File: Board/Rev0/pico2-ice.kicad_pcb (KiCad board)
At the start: 4 copper layers, 27.9 x 63.5 mm, 119 parts, among them J1 USB_C_Receptacle_USB2.0, J2 Conn_02x20_Odd_Even, J3 Conn_02x20_Odd_Even, J4 PB_SEL, J5 SM03B-SRSS-TB, J6 Conn_01x22_MountingPin, SW1 PTS820 J25K SMTR LFS, SW2 PTS820 J25K SMTR LFS, U1 NCP115AMX120TCG, U2 W25Q32JVSSIQ, U3 RP2350_80QFN, U4 TL431DBZ, U5 APS6404L-3SQN-SN, U6 ICE40UP5K-SG48ITR, U8 W25Q32JVSSIQ, U9 NCP115AMX330TCG, Y1 ABM8-272-T3

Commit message: Update the design with feedbacks.
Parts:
- SW1, SW2: value PTS820 J25K SMTR LFS -> CS1213AGF260
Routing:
- net GND: track 76.8 -> 78.0 mm, vias 73 -> 71

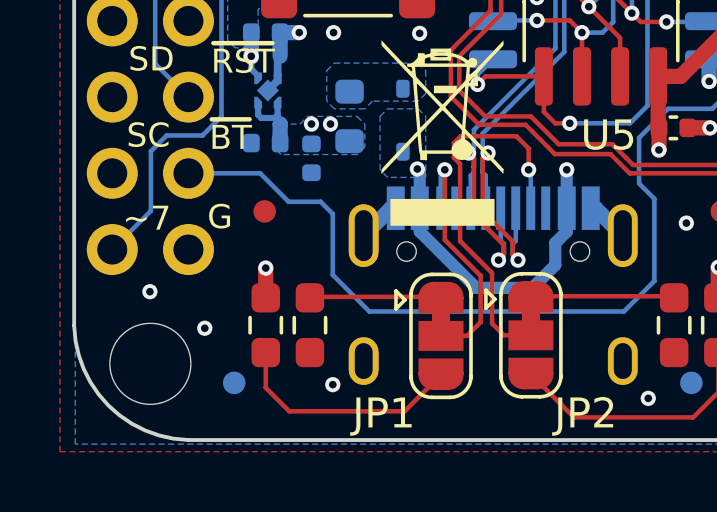
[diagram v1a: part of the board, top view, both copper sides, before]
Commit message: Minor silkscreen edits
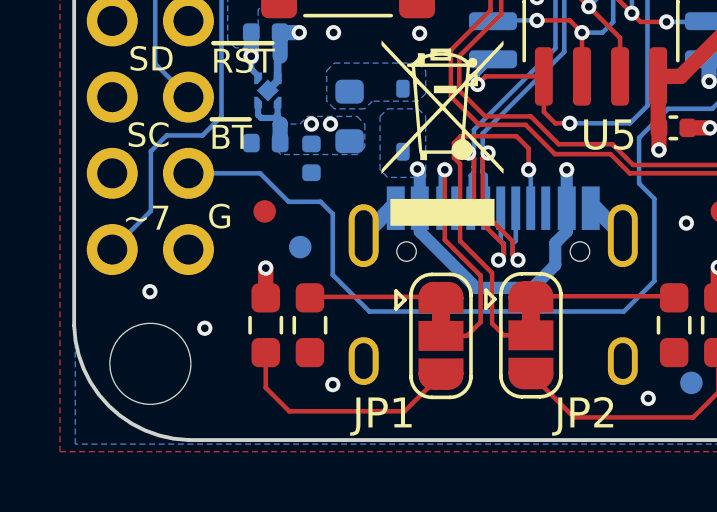
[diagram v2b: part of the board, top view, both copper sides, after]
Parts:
- moved FID6 5.03 mm to (66.0, 128.2)
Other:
- board text added: "pico2-ice"
- board text added: "rev1"
- board text removed: "pico-ice"
- board text removed: "pico-ice v1"
- board text removed: "rev3"
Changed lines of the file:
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@@
 	(footprint "Fiducial:Fiducial_0.75mm_Mask1.5mm"
 		(layer "B.Cu")
-		(at 63.754 132.715 180)
+		(at 65.955718 128.189071 180)
 		(descr "Circular Fiducial, 0.75mm bare copper, 1.5mm soldermask opening (Level B)")
 		(tags "fiducial")
@@
 		)
 	)
-	(gr_text "pico-ice"
-		(at 66.024918 130.386271 270)
+	(gr_text "pico2-ice"
+		(at 63.955718 130.689071 90)
 		(layer "B.Mask")
 		(effects
 			(font
-				(size 1.016 1.016)
-				(thickness 0.254)
-				(bold yes)
+				(size 0.9 0.9)
+				(thickness 0.127)
 			)
 			(justify mirror)
 		)
 	)
-	(gr_text "rev3"
-		(at 64.450118 129.167071 270)
+	(gr_text "rev1"
+		(at 65.955718 131.189071 90)
 		(layer "B.Mask")
 		(effects
 			(font
-				(size 1.016 1.016)
-				(thickness 0.254)
-				(bold yes)
+				(size 0.9 0.9)
+				(thickness 0.127)
 			)
 			(justify mirror)
 		)
 	)
-	(gr_text "pico-ice v1"
+	(gr_text "pico2-ice"
 		(at 78.470918 76.385871 0)
 		(layer "F.Mask")
@@
 			(font
 				(size 0.9 0.9)
-				(thickness 0.225)
-				(bold yes)
+				(thickness 0.1125)
 			)
 		)

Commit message: Sync the latest files.
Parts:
- removed J4: PB_SEL, Jumper:SolderJumper-3_P1.3mm_Bridged12_RoundedPad1.0x1.5mm_NumberLabels
- removed R14: 2.2K, Resistor_SMD:R_0402_1005Metric
- added D6: 1N5819WS, Diode_SMD:D_SOD-323, F.Cu at (96.1, 109.9)
- added R32: 10K, Resistor_SMD:R_0402_1005Metric, F.Cu at (92.4, 109.4)
- added R33: 5.1K, Resistor_SMD:R_0603_1608Metric_Pad0.98x0.95mm_HandSolder, F.Cu at (96.1, 112.6)
- added R34: 27, Resistor_SMD:R_0402_1005Metric, F.Cu at (92.4, 111.4)
- C13, C32, D2, D3, D4, J1, RN1, SW1, SW2: moved to F.Cu
- JP1, JP2, U8: moved to B.Cu
- R30, R31: footprint Resistor_SMD:R_0402_1005Metric -> Jumper:SolderJumper-2_P1.3mm_Bridged_RoundedPad1.0x1.5mm
- moved SW1 25.4 mm to (67.7, 122.8)
- moved LOGO3 24.0 mm to (97.1, 82.9)
- moved R30 23.0 mm to (95.2, 120.2)
- moved R31 22.6 mm to (95.3, 117.3)
- moved LOGO2 21.3 mm to (91.4, 129.2)
- moved LOGO4 15.9 mm to (92.6, 137.3)
- moved LOGO1 14.9 mm to (92.6, 72.4)
- moved FID3 14.3 mm to (57.4, 139.2)
- moved FID1 13.1 mm to (84.9, 139.1)
- moved FID6 12.3 mm to (60.4, 139.1)
- moved FID5 8.94 mm to (54.8, 74.3)
- moved JP2 8.86 mm to (73.4, 140.0)
- moved C26 8.84 mm to (73.9, 76.4), turned to 0 degrees
- moved JP1 8.27 mm to (67.5, 138.8)
- moved FID4 7.27 mm to (82.6, 139.0)
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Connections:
- J6 pad 11: /Lane2_N -> /Lane2_P
- J6 pad 12: /Lane2_P -> /Lane2_N
- R2 pad 2: /~{USB_BOOT} -> Net-(D6-A)
- R27 pad 2: /~{RP_SRAM_SS} -> /~{SRAM_SS}
- SW1 pad 2: Net-(J4-Pin_2) -> /~{USB_BOOT}
- U3 pad 11: /Lane2_N -> /Lane2_P
- U3 pad 12: /Lane2_P -> /Lane2_N
- U3 pad 22: /ICE_21 -> Net-(U3-GPIO22)
- U3 pad 27: /ICE_20_G3 -> /ICE_21
- U3 pad 36: /PICO_PMOD_A3 -> /ICE_9
- U3 pad 37: /PICO_PMOD_A1 -> /ICE_11
- U3 pad 38: /PICO_PMOD_A4 -> /ICE_25
- U3 pad 39: /PICO_PMOD_A2 -> /~{ICE_RST}
- U3 pad 40: /PICO_PMOD_B3 -> /PICO_PMOD_A3
- U3 pad 42: /PICO_PMOD_B1 -> /PICO_PMOD_A1
- U3 pad 43: /PICO_PMOD_B4 -> /PICO_PMOD_A4
- U3 pad 44: /PICO_PMOD_B2 -> /PICO_PMOD_A2
- U3 pad 45: /ICE_9 -> /PICO_PMOD_B3
- U3 pad 46: /ICE_11 -> /PICO_PMOD_B1
- U3 pad 47: /ICE_25 -> /PICO_PMOD_B4
- U3 pad 48: /~{ICE_RST} -> /PICO_PMOD_B2
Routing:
- net GND: track 78.0 -> 47.8 mm, vias 71 -> 61
- net /LED_B: track 44.2 -> 29.6 mm, vias 2 -> 1
- net /ICE_LED_G: track 47.7 -> 33.5 mm
- net /LED_G: track 42.6 -> 28.5 mm
- net Net-(J1-CC1): track 12.8 -> 0.00 mm, vias 1 -> 0
- net /USB_D+: track 25.7 -> 13.1 mm, vias 2 -> 0
- net /USB_D-: track 25.7 -> 13.2 mm, vias 2 -> 0
- net /ICE_LED_B: track 49.0 -> 36.6 mm
- net /LED_R: track 42.0 -> 29.8 mm
- net Net-(J4-Pin_2): track 12.0 -> 0.00 mm
- net V_{BUS}: track 27.2 -> 16.2 mm
- net /ICE_SI: track 58.3 -> 47.4 mm, vias 2 -> 1
- net /ICE_SCK: track 67.2 -> 57.3 mm, vias 4 -> 3
- net /ICE_13|IO3: track 25.1 -> 15.6 mm, vias 3 -> 1
- net Net-(J1-CC2): track 8.42 -> 0.00 mm, vias 1 -> 0
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
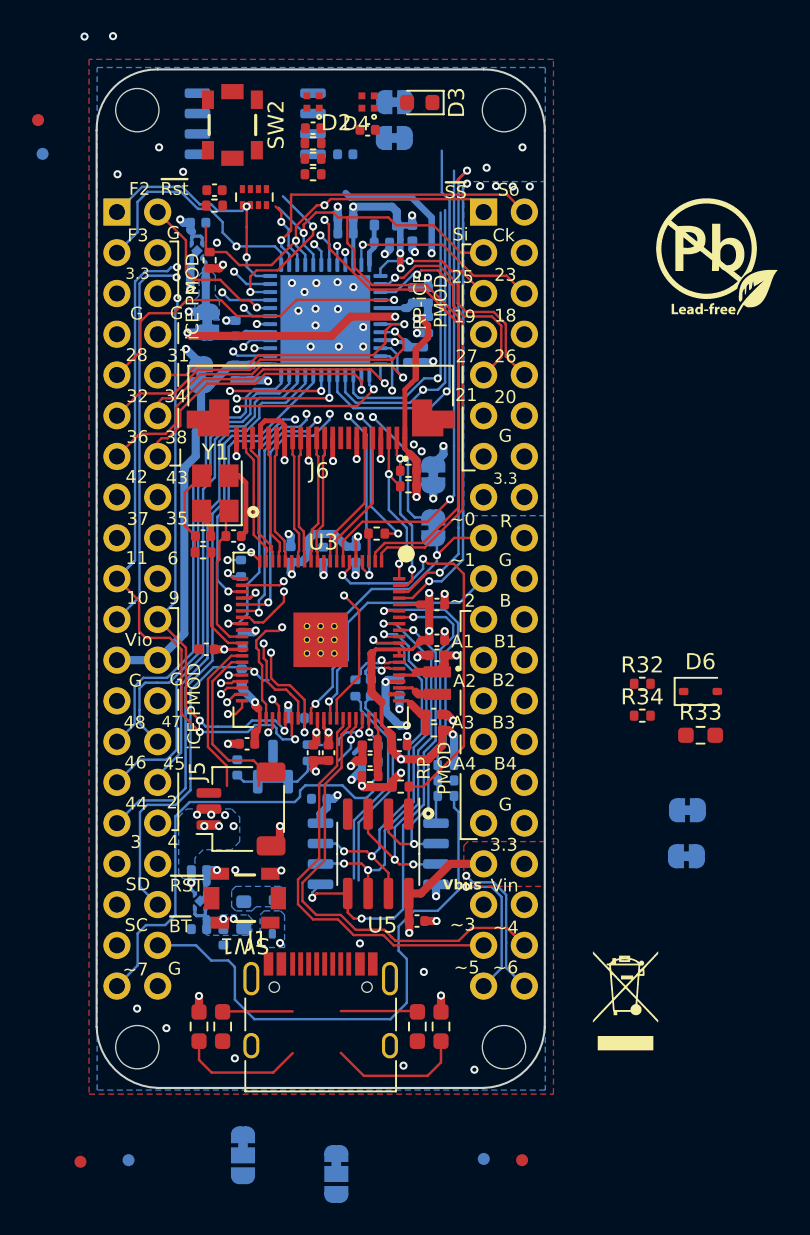
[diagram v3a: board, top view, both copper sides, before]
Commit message: Complete the layout update for a review.
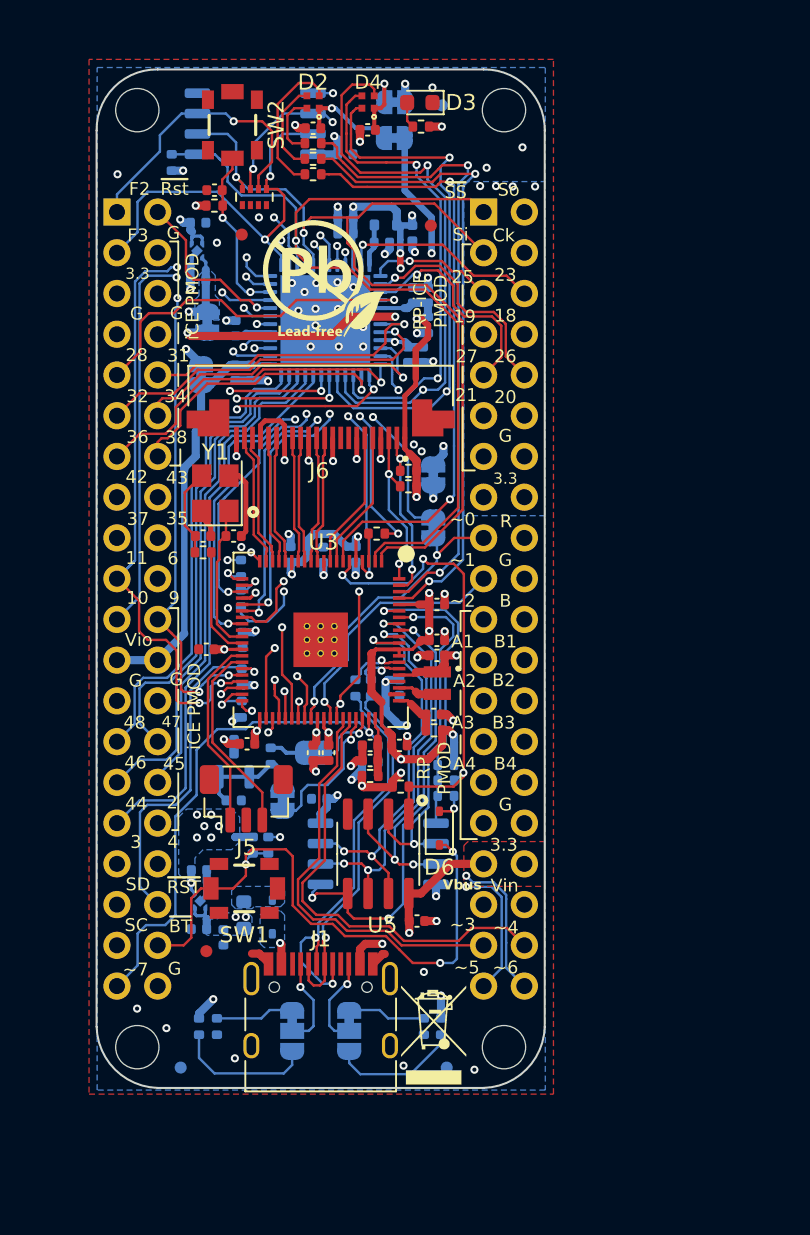
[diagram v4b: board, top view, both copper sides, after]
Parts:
- added R14: 2.2K, Resistor_SMD:R_0402_1005Metric, F.Cu at (78.6, 74.7)
- J5: value SM03B-SRSS-TB -> BM03B-SRSS-TB; footprint Connector_JST:JST_SH_SM03B-SRSS-TB_1x03-1MP_P1.00mm_Horizontal -> Connector_JST:JST_SH_BM03B-SRSS-TB_1x03-1MP_P1.00mm_Vertical
- R10, R20, R22, R24, R33: footprint Resistor_SMD:R_0603_1608Metric_Pad0.98x0.95mm_HandSolder -> Resistor_SMD:R_0402_1005Metric; moved to B.Cu
- R32, R34, R8: moved to B.Cu
- moved LOGO1 64.4 mm to (64.3, 130.2), turned to 90 degrees
- moved FID1 58.5 mm to (79.3, 80.9)
- moved R33 27.8 mm to (69.1, 119.5), turned to 90 degrees
- moved R32 26.3 mm to (68.2, 119.5), turned to -90 degrees
- moved R34 26.1 mm to (67.4, 104.1), turned to 90 degrees
- moved R30 25.4 mm to (70.0, 116.7), turned to -90 degrees
- moved FID2 25.1 mm to (79.9, 73.4)
- moved LOGO3 24.6 mm to (72.6, 84.3)
- moved R31 23.6 mm to (71.9, 113.7)
- moved LOGO4 21.0 mm to (76.3, 124.1), turned to 0 degrees
- moved D6 18.4 mm to (79.8, 118.4), turned to 90 degrees
- moved FID3 15.3 mm to (65.3, 126.1)
- moved R20 15.1 mm to (79.9, 130.8)
- moved R22 15.1 mm to (64.8, 130.8)
- moved FID5 14.6 mm to (67.5, 81.4)
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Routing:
- net /ICE_LED_B: track 36.6 -> 52.4 mm, vias 1 -> 2
- net /ICE_12|IO2: track 14.9 -> 29.5 mm
- net /USB_D+: track 13.1 -> 25.5 mm, vias 0 -> 2
- net /ICE_LED_G: track 33.5 -> 45.9 mm, vias 1 -> 2
- net /LED_G: track 28.5 -> 39.8 mm
- net /ADC2|PB: track 18.2 -> 29.0 mm, vias 1 -> 3
- net /ICE_SO: track 48.7 -> 59.4 mm, vias 3 -> 4
- net /ICE_SI: track 47.4 -> 57.9 mm, vias 1 -> 2
- net /LED_R: track 29.8 -> 39.8 mm
- net /ICE_13|IO3: track 15.6 -> 25.4 mm, vias 1 -> 2
- net /USB_D-: track 13.2 -> 22.9 mm, vias 0 -> 1
- net /ICE_LED_R: track 36.5 -> 45.7 mm, vias 1 -> 2
- net Net-(D2-BK): track 0.00 -> 9.18 mm
- net /PICO_PMOD_A2: track 26.9 -> 18.4 mm
- net /LED_B: track 29.6 -> 37.5 mm, vias 1 -> 2
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
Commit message: Updated layout with some grounds, fixed BoM
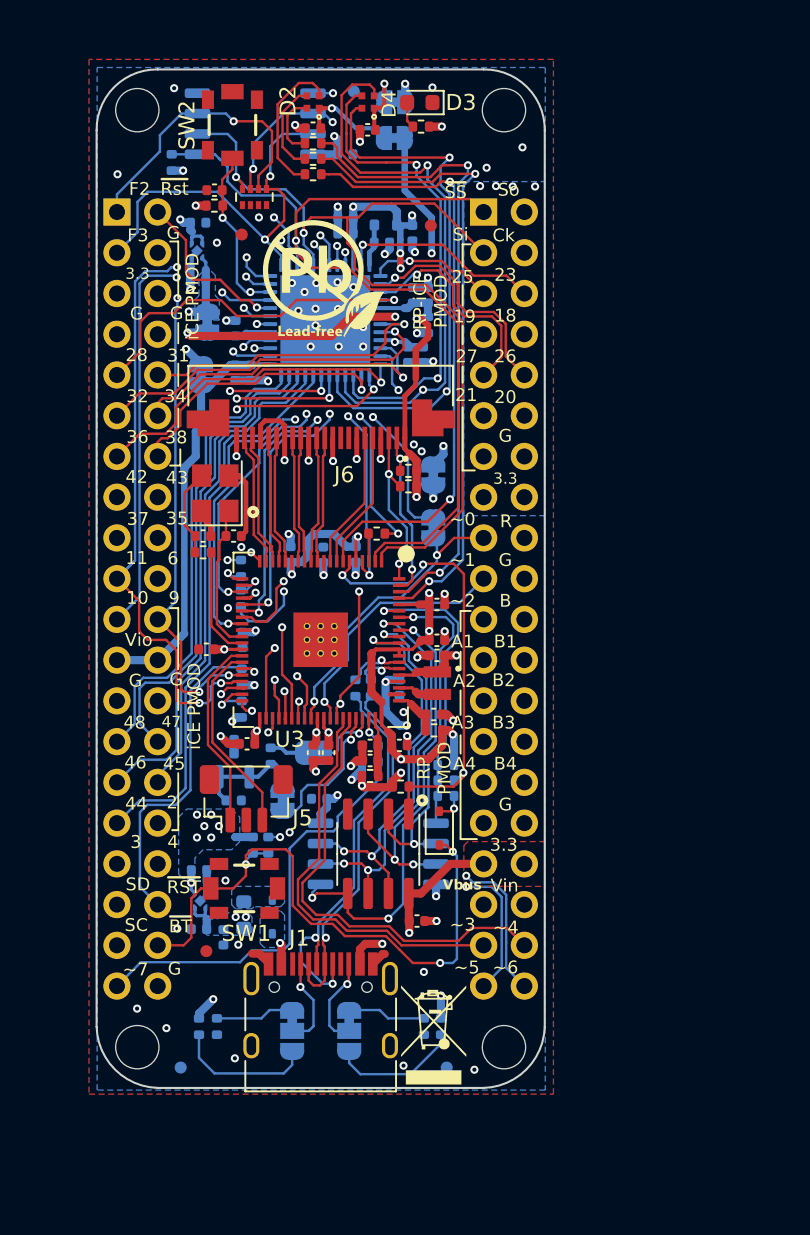
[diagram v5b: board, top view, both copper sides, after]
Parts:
- moved FID2 5.56 mm to (74.5, 72.5)
- moved LOGO1 0.32 mm to (64.3, 129.9)
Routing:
- net /ADC7: track 32.2 -> 29.6 mm
- net GND: vias 56 -> 62
